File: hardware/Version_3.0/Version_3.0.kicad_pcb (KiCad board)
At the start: 2 copper layers, 21.4 x 21.7 mm, 45 parts, among them J1 Conn_01x05, J2 Conn_01x05, J3 Conn_Coaxial, U1 ADF4351, Y1 SG-5032CAN

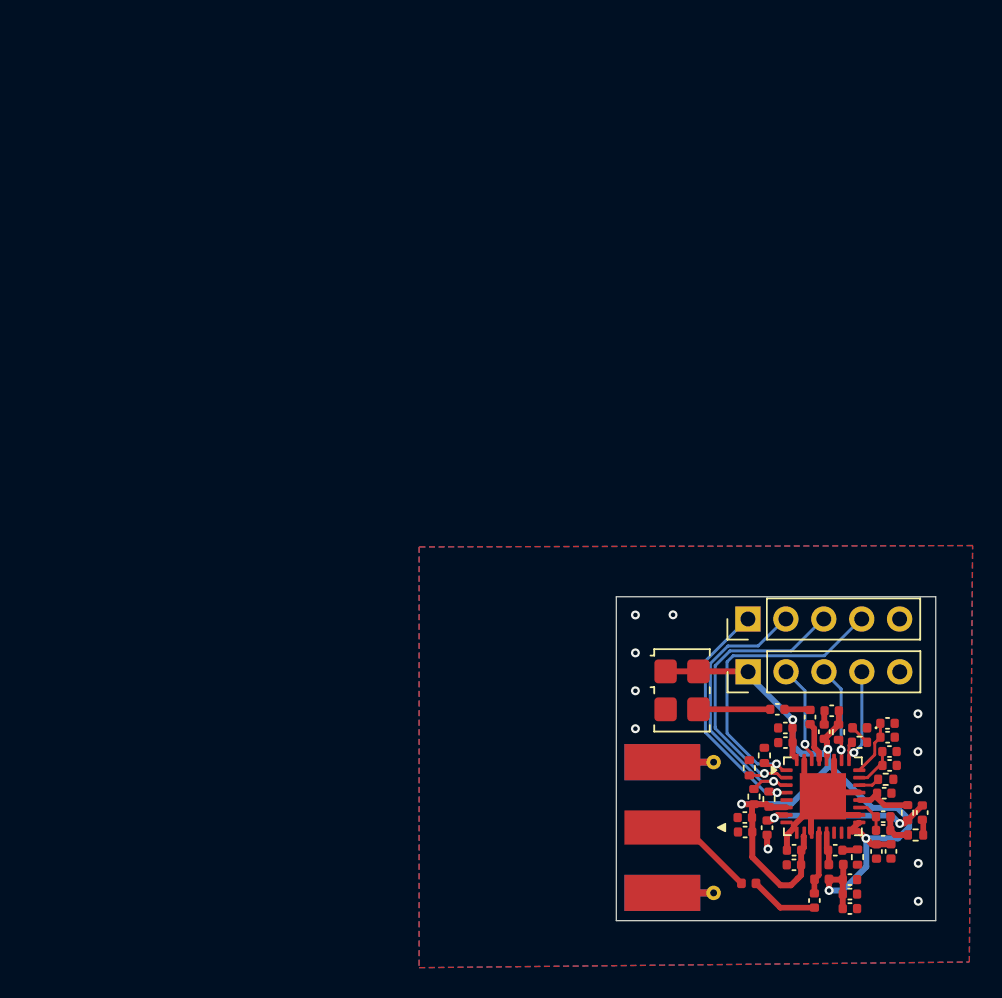
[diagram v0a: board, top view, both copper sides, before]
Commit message: changed the pin header connectors for version 3 board
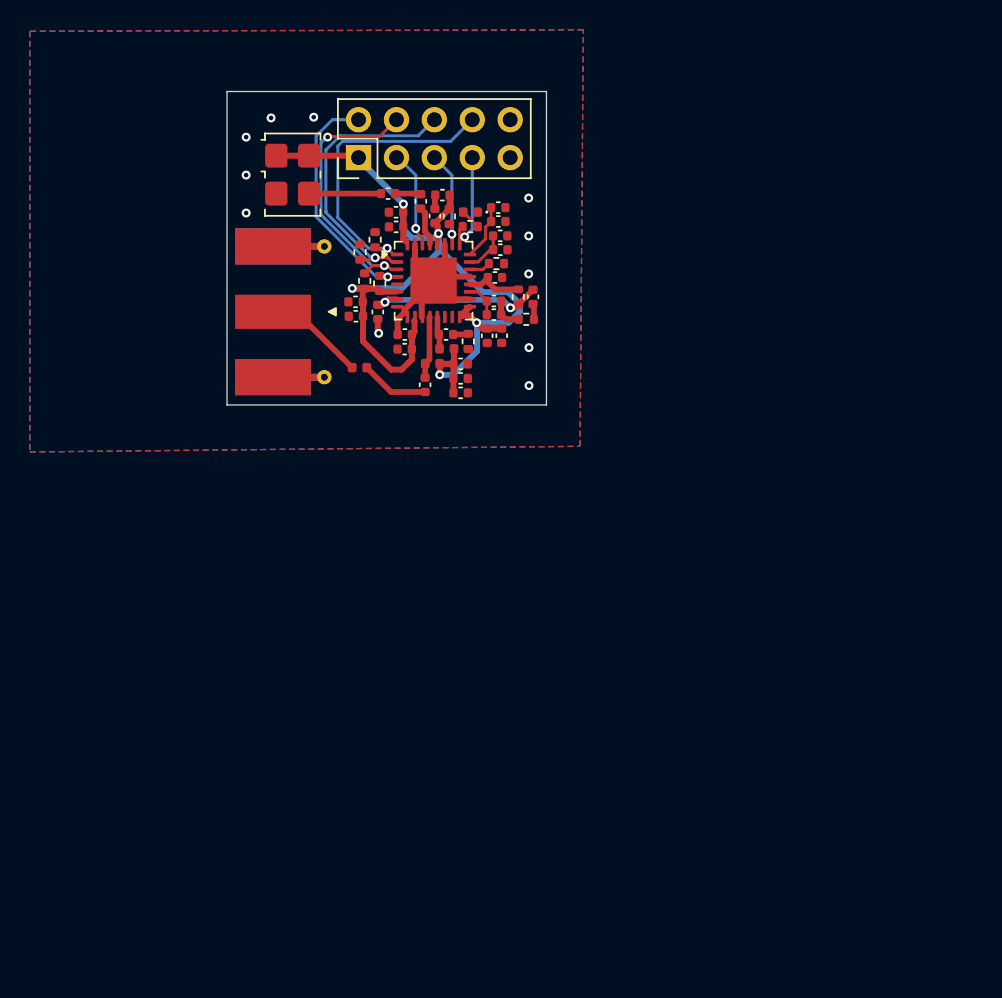
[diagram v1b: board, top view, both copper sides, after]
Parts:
- removed the J2 at (133.2, 93.6)
- J1: value Conn_01x05 -> Conn_02x05_Counter_Clockwise; footprint Connector_PinHeader_2.54mm:PinHeader_1x05_P2.54mm_Vertical -> Connector_PinHeader_2.54mm:PinHeader_2x05_P2.54mm_Vertical
- moved R5 43.3 mm to (108.5, 67.6)
- moved C10 43.3 mm to (109.6, 63.8)
- moved C12 43.3 mm to (113.9, 75.0)
- moved C13 43.3 mm to (113.9, 74.0)
- moved C16 43.3 mm to (111.2, 62.1)
- moved C17 43.3 mm to (112.9, 71.0)
- moved C2 43.3 mm to (116.7, 71.1)
- moved C21 43.3 mm to (116.6, 64.4)
- moved C22 43.3 mm to (116.4, 63.5)
- moved C23 43.3 mm to (116.4, 62.5)
- moved C26 43.3 mm to (116.2, 67.2)
- moved C8 43.3 mm to (109.6, 62.9)
- moved C9 43.3 mm to (106.9, 68.9)
- moved J2 43.3 mm to (103.1, 69.5)
- moved L2 43.3 mm to (112.0, 73.0)
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- renumbered J3 to J2
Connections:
- J1 pad 1: CE -> +3.3V
- J1 pad 2: CS -> CE
- J1 pad 3: MOSI -> MUXOUT
- J1 pad 4: CLK -> CS
- J1 pad 5: GND -> PDB_RF
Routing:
- net CS: track 19.2 -> 18.9 mm, vias 1 -> 2
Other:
- board size 21.4 x 21.7 mm -> 21.4 x 21 mm

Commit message: updated pcb to 4 layers and the images. this is for v3
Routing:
- net +3.3V: track 67.4 -> 64.0 mm
- added copper zone on In1.Cu, net GND
- added copper zone on In2.Cu, net GND
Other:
- copper layers 2 -> 4

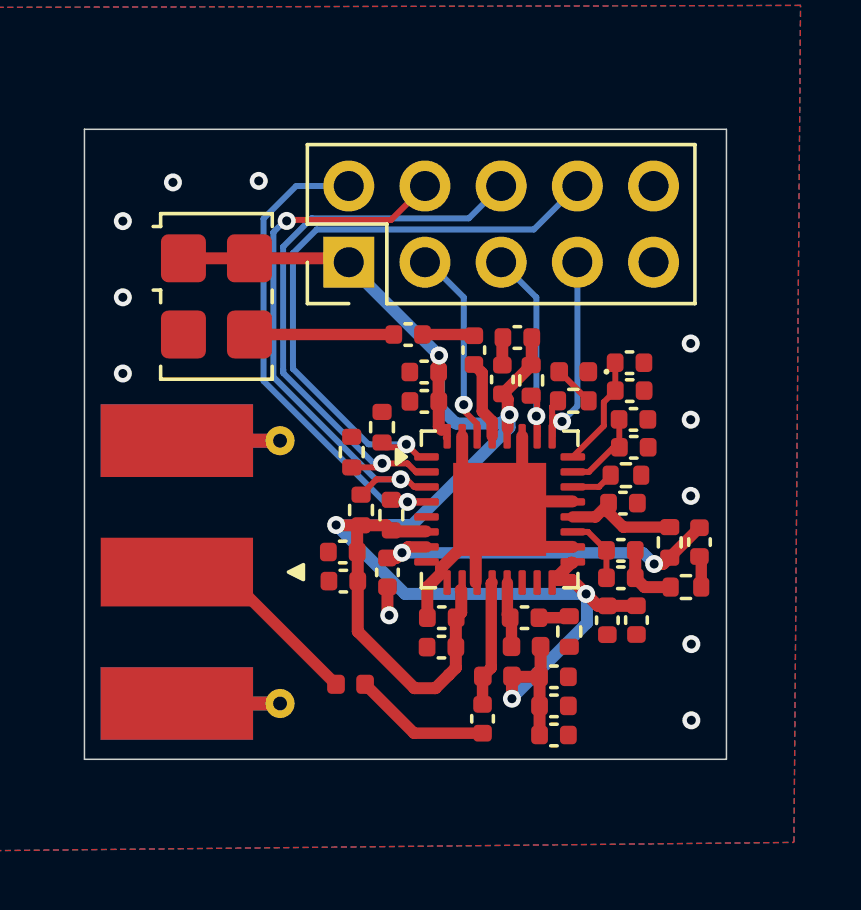
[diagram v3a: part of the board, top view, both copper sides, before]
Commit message: Correct V3 header wiring and PCB routing
Update the Version 3 schematic and board with the corrected header pinout, ground connections, and signal routing. Refresh board figures and add PCBWay Gerber and IPC netlist production files.
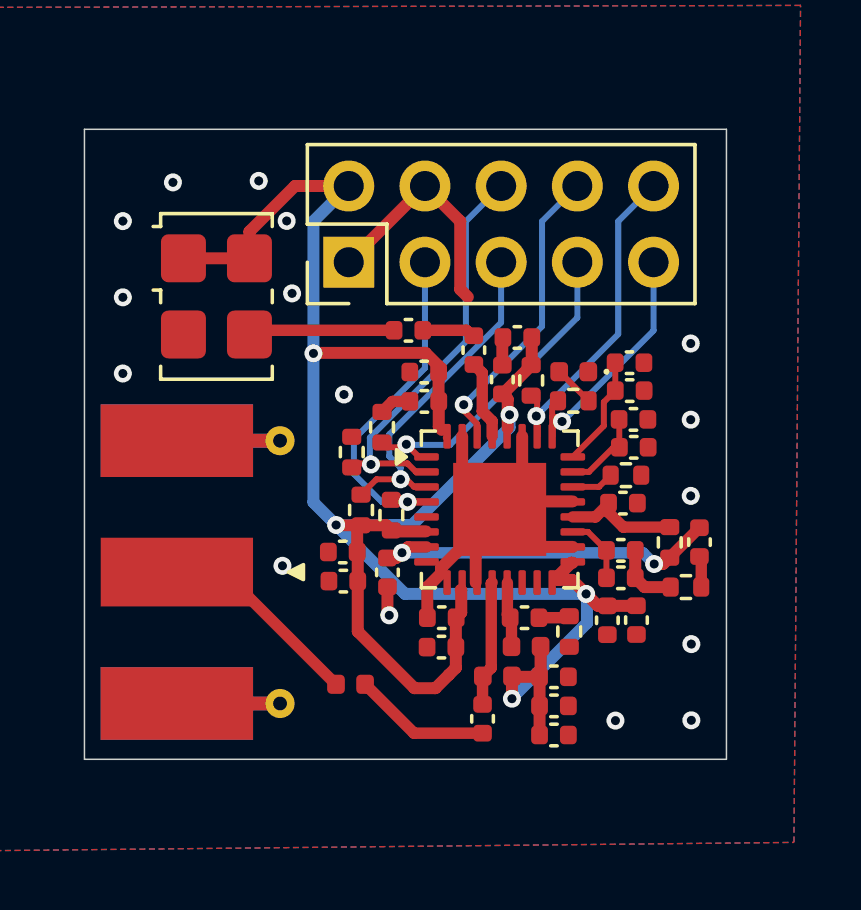
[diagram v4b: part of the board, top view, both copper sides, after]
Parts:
- moved C15 0.14 mm to (109.1, 61.5)
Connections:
- J1 pad 1: +3.3V -> GND
- J1 pad 10: GND -> PDB_RF
- J1 pad 2: CE -> +3.3V
- J1 pad 3: MUXOUT -> CE
- J1 pad 4: CS -> GND
- J1 pad 5: PDB_RF -> CS
- J1 pad 7: LD -> CLK
- J1 pad 8: CLK -> MUXOUT
- J1 pad 9: GND -> LD
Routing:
- net GND: track 22.7 -> 41.5 mm, vias 11 -> 16
- net CLK: track 20.6 -> 10.8 mm
- net +3.3V: track 64.0 -> 72.8 mm
- net CS: track 18.9 -> 11.4 mm, vias 2 -> 1
- net MOSI: track 20.0 -> 14.0 mm
- net CE: track 16.4 -> 11.4 mm
- net PDB_RF: track 7.17 -> 10.8 mm
- net MUXOUT: track 6.60 -> 10.1 mm
- net LD: track 7.29 -> 8.24 mm
